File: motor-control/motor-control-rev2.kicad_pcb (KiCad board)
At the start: 2 copper layers, 122.3 x 65.9 mm, 89 parts, among them P1 CONN_02X12, P2 to_motor_phase_1, P3 to_motor_phase_2, P4 to_motor_phase_3, P5 CONN_01X01, P6 CONN_01X01, P7 CONN_01X04, Q1 csd19505kcs, Q10 csd19505kcs, Q11 csd19505kcs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

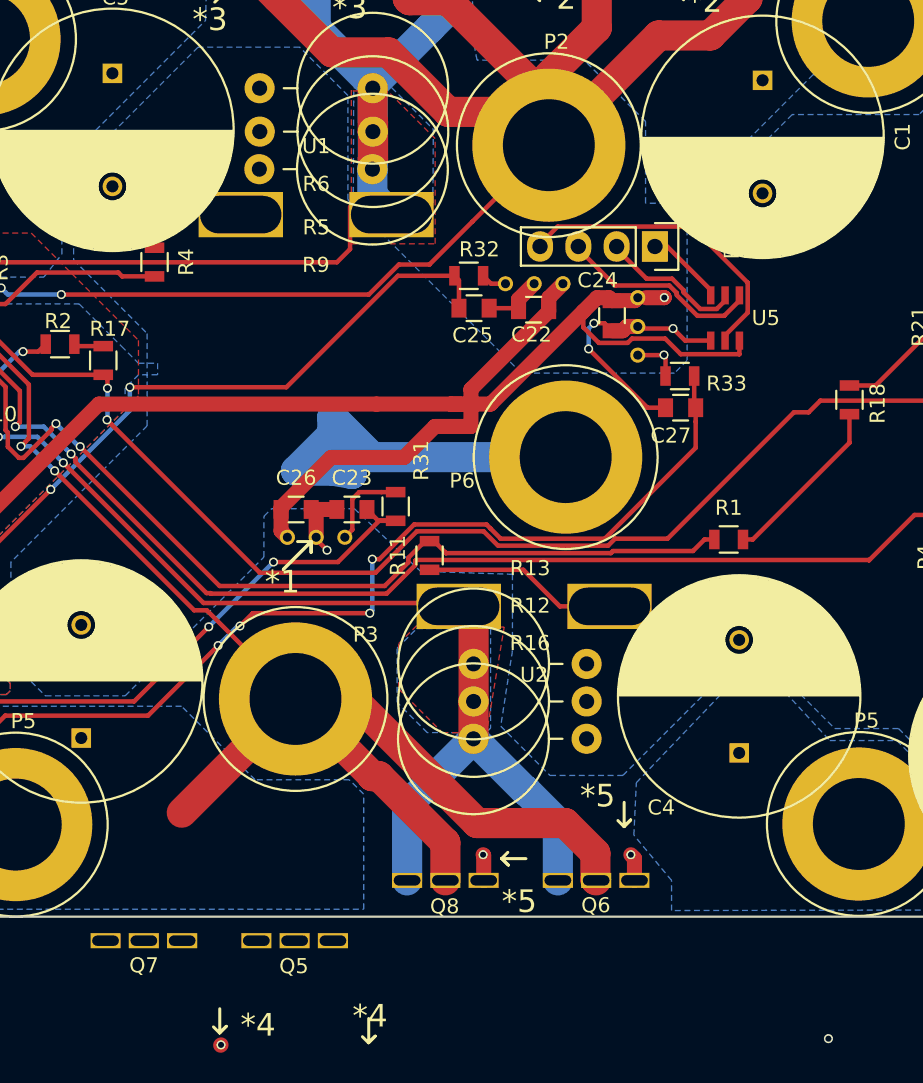
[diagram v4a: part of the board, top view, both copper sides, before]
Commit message: Finished up bottom fets
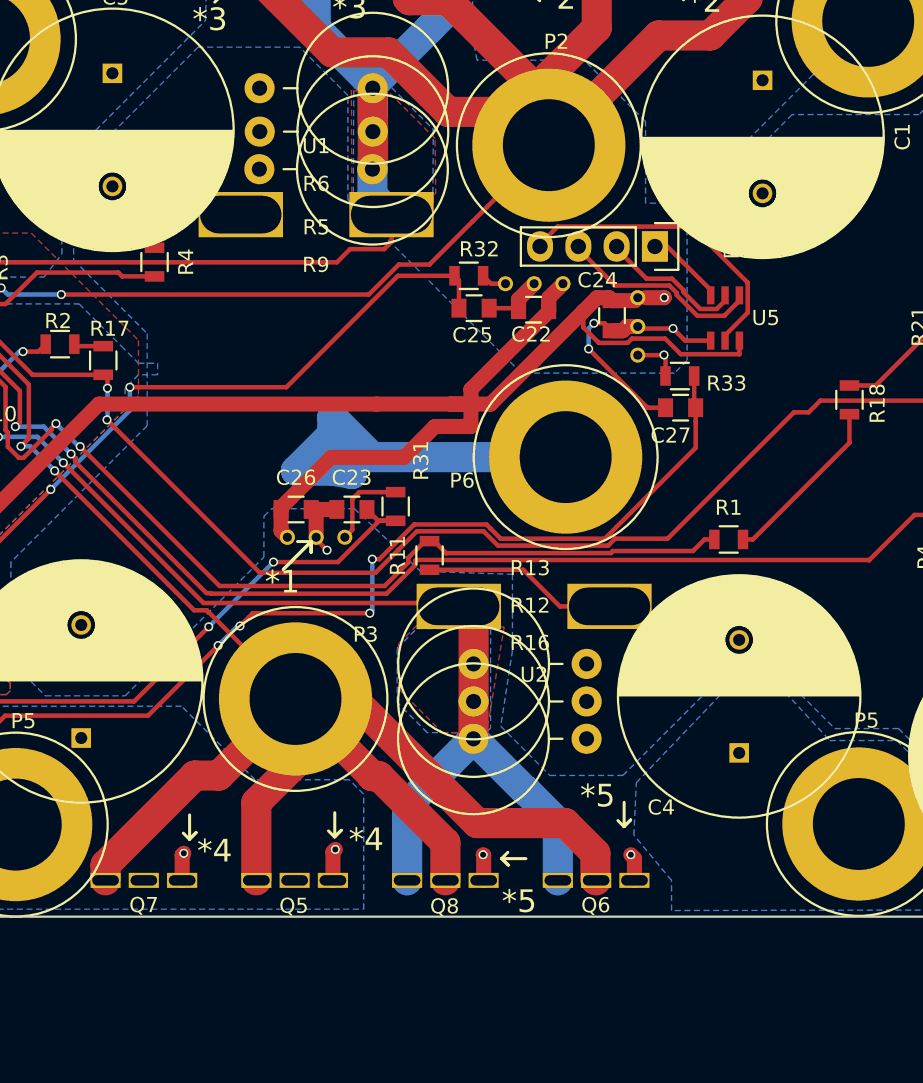
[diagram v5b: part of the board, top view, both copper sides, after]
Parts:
- moved Q5 4.00 mm to (150.0, 118.0)
- moved Q7 4.00 mm to (140.0, 118.0)
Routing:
- net /Gate-Driver/SH_B: track 104.6 -> 125.3 mm
- net Net-(Q5-Pad1): track 2.50 -> 6.46 mm, vias 2 -> 4
- net /Gate-Driver/SL_A: track 81.9 -> 83.8 mm
- net (no net): track 1.26 -> 1.22 mm, vias 3 -> 1

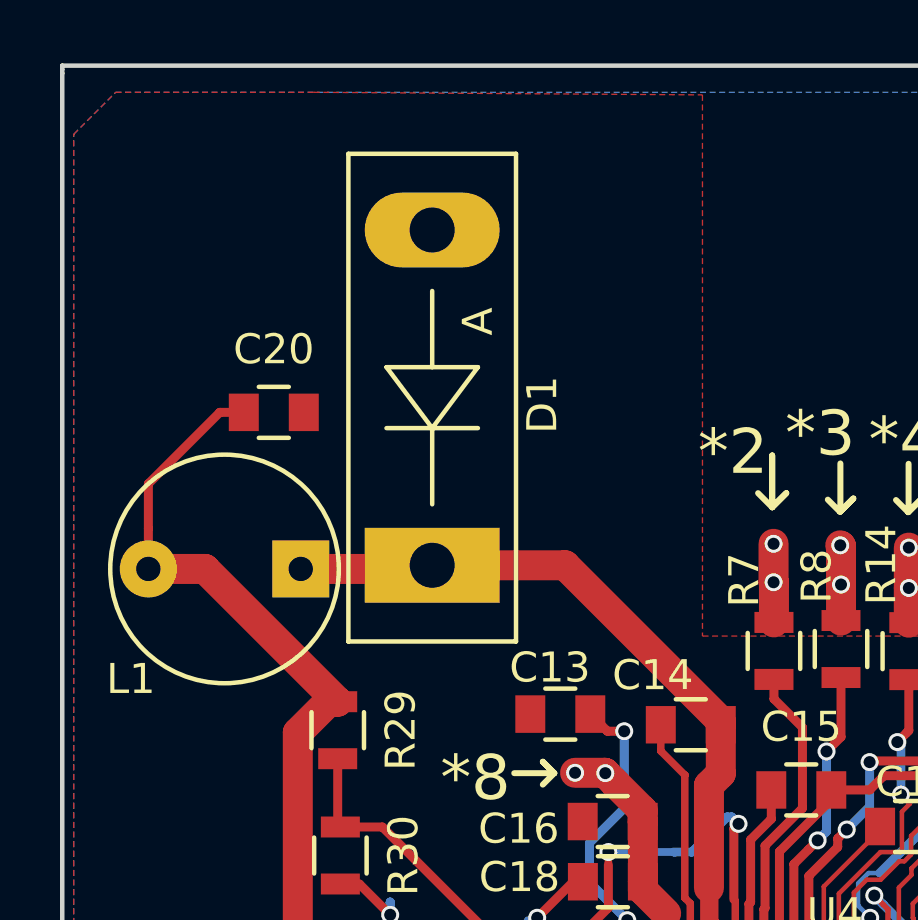
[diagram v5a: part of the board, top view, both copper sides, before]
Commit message: Updated pcb diode and inductor, placed them
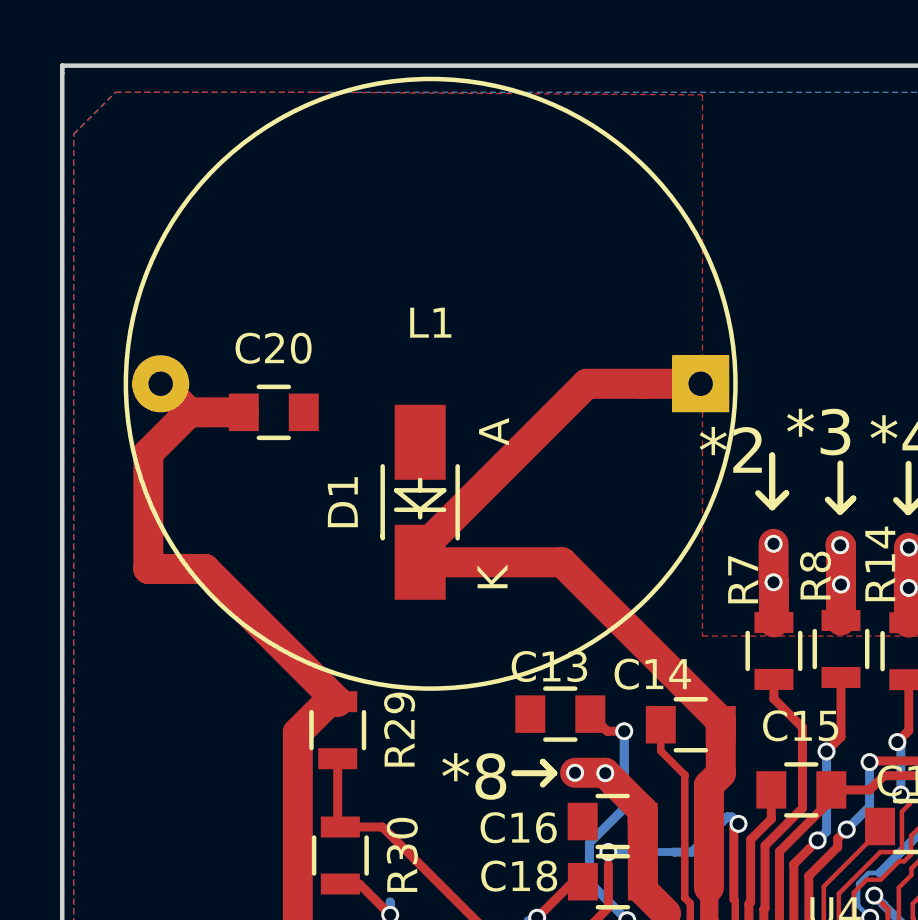
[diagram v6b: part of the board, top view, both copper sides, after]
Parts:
- C16: value 0.1uF -> DNP
- C18: value 4.7uF -> 10uF
- C20: value 47uF -> 22uF
- C21: value 4.7uF -> 1uF
- C7: value 2700 pF -> 10pF
- C8: value 6.8 pF -> 0.01uF
- D1: footprint Diodes_ThroughHole:Diode_TO-247_Vertical -> p16261:B220A-13-F
- L1: value 22uH -> 68uH; footprint Inductors:INDUCTOR_V -> p16261:PHC-27-683
- R24: value 76.8k -> 24.3k
- R27: value 800k -> 205k
- R29: value 22k -> 53.6k
- R30: value 4k -> 10k
- moved L1 9.24 mm to (102.7, 65.1)
- moved D1 2.13 mm to (102.3, 69.0)
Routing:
- net Net-(C14-Pad2): track 29.7 -> 37.8 mm
- net VCC: track 183.2 -> 186.0 mm

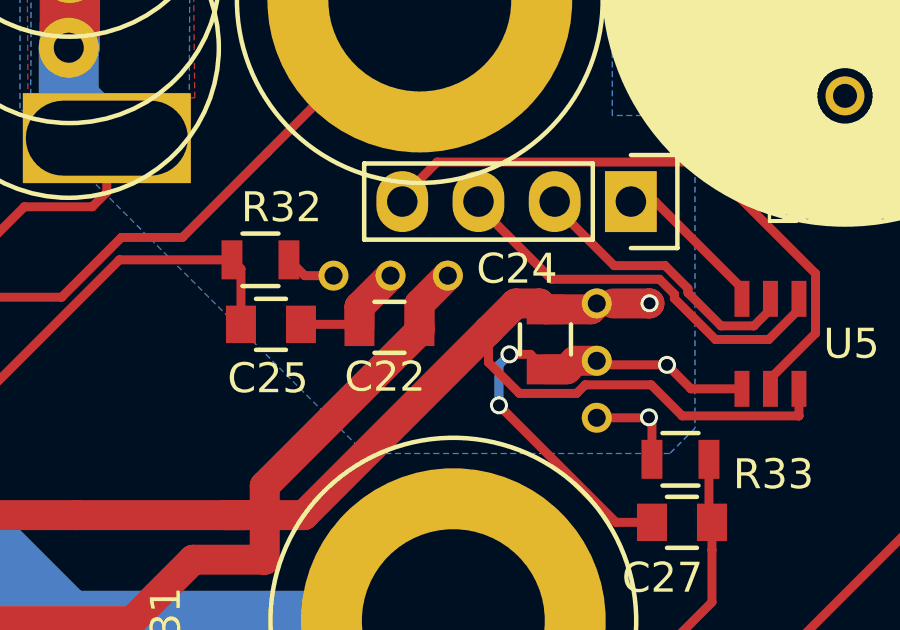
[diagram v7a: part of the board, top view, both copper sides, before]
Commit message: Fixd*1 ground(hall): added trace to other hall gnd
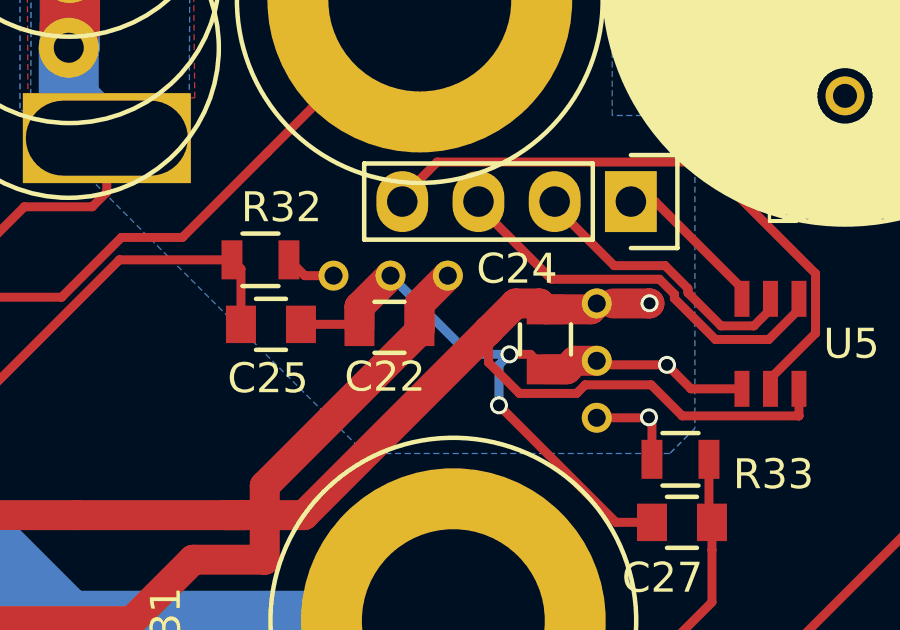
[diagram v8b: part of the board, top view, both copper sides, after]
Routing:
- net GND: track 118.3 -> 123.4 mm
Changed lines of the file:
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@@
     (thickness 1.6)
     (drawings 140)
-    (tracks 1358)
+    (tracks 1360)
     (zones 0)
     (modules 89)
@@
   )
   (setup
-    (last_trace_width 0.1524)
+    (last_trace_width 0.3)
     (user_trace_width 0.18)
     (user_trace_width 0.3)
@@
   (segment (start 109.7238 81.9778) (end 110.4985 82.7525) (width 1) (layer F.Cu) (net 1))
   (segment (start 109.7238 81.6984) (end 109.7238 81.9778) (width 1) (layer F.Cu) (net 1))
+  (segment (start 165.8853 78.4274) (end 168.5079 81.05) (width 0.3) (layer B.Cu) (net 2))
+  (segment (start 168.5079 81.05) (end 169.85 81.05) (width 0.3) (layer B.Cu) (net 2))
   (segment (start 165.1679 97.4) (end 167.5953 99.8274) (width 0.3) (layer F.Cu) (net 2))
   (segment (start 167.5953 99.8274) (end 170.8853 99.8274) (width 0.3) (layer F.Cu) (net 2))
